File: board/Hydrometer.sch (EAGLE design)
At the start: 13 parts, among them IC2 REG1117

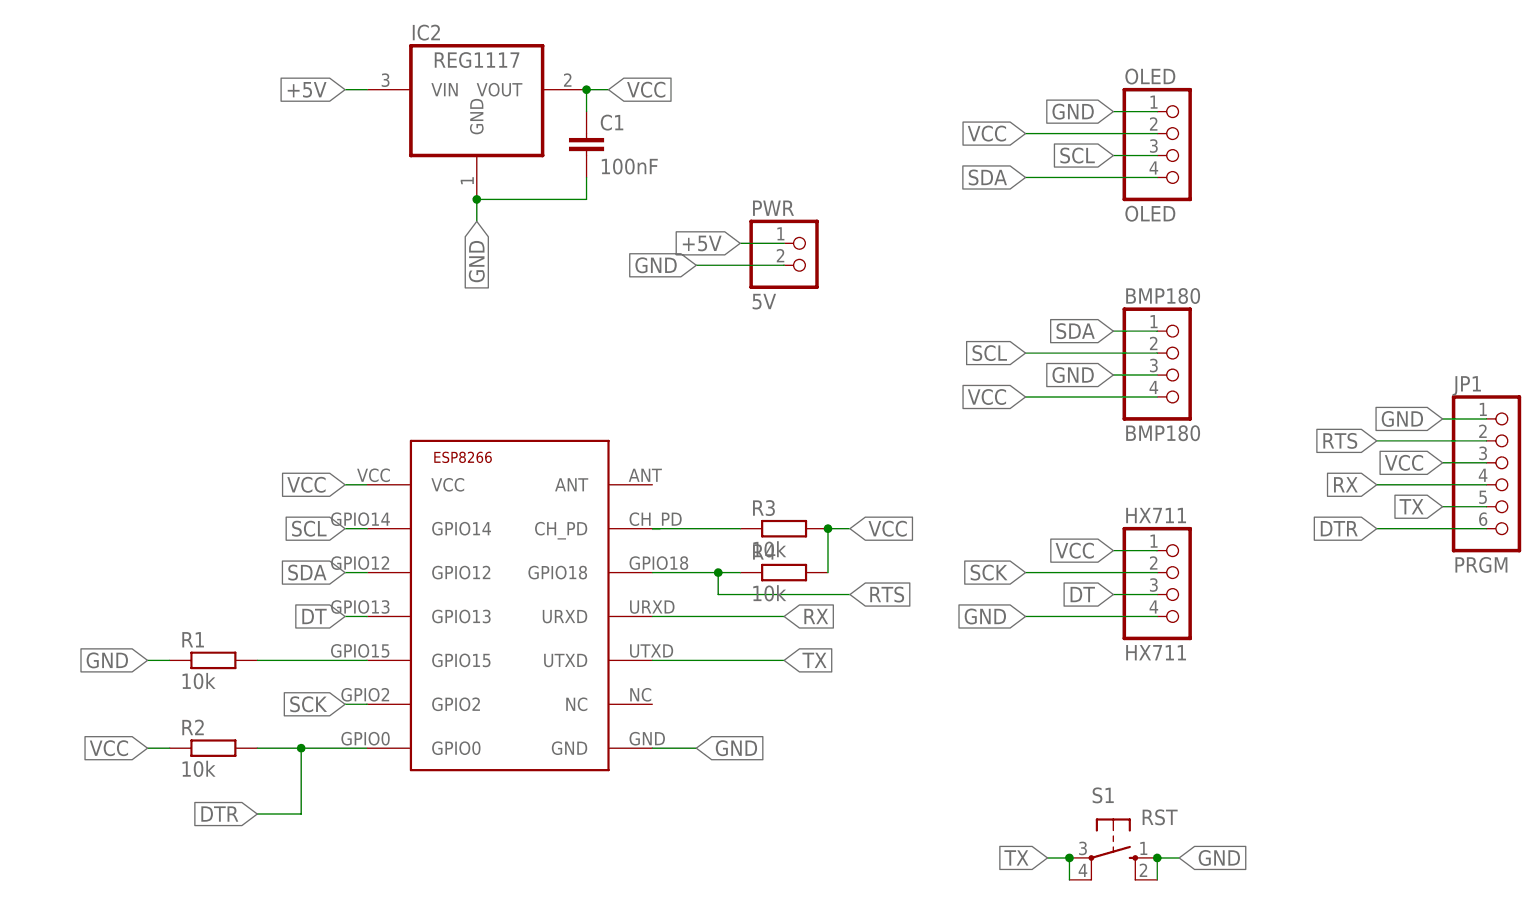
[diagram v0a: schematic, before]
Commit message: Update board layout to a (mostly) single sided PCB
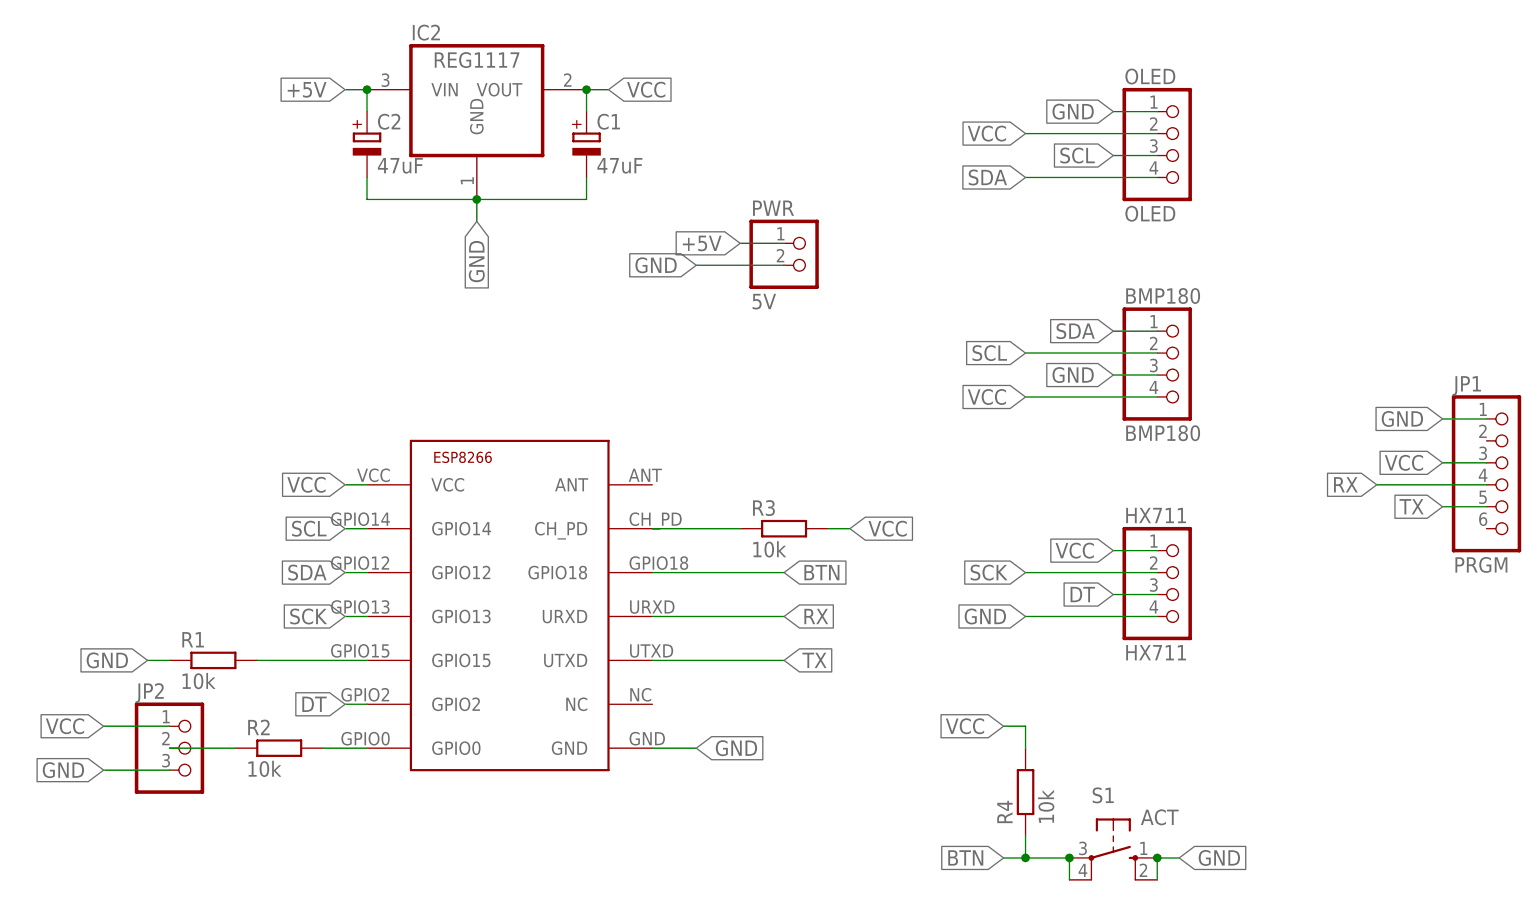
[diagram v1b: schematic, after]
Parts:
- added C2: 47uF, resistor:CPOL-EUE2.5-5
- added JP2: (no value), pinhead:PINHD-1X3
- C1: value 100nF -> 47uF; device resistor:C-EUC1206 -> resistor:CPOL-EUE2-5
- R1, R2, R3, R4: device resistor:R-EU_M1206 -> resistor:R-EU_R1206
- S1: value RST -> ACT
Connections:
- removed net RTS: JP1.2, R4.1, U$1.GPIO18
- new net BTN: R4.1, S1.P, S1.P1, U$1.GPIO18
- new net N$2: JP2.2, R2.1
- net +5V: now also C2.+
- net DT: now also U$1.GPIO2; no longer U$1.GPIO13
- net DTR: no longer JP1.6
- net GND: now also C1.-, C2.-, JP2.3; no longer C1.2
- net SCK: now also U$1.GPIO13; no longer U$1.GPIO2
- net TX: no longer S1.P, S1.P1
- net VCC: now also C1.+, JP2.1; no longer C1.1, R2.1
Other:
- moved on the sheet: R2, R4

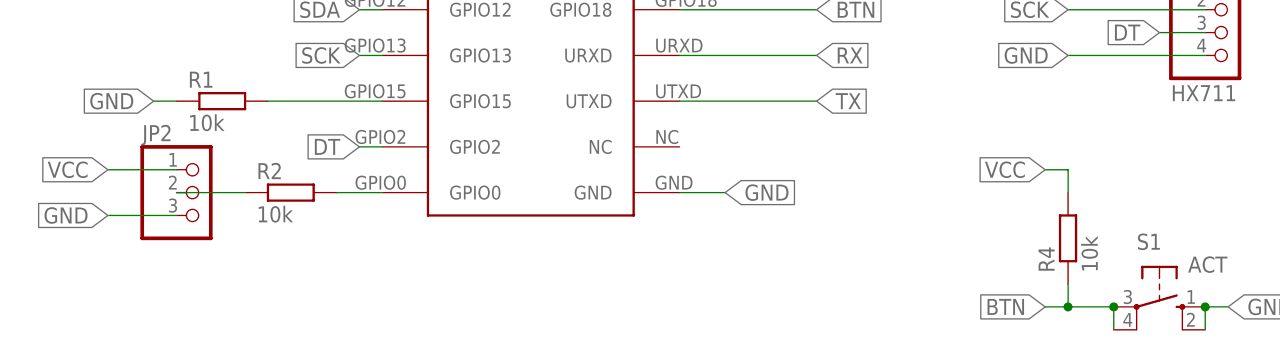
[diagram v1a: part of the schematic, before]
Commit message: Add fill planes to board
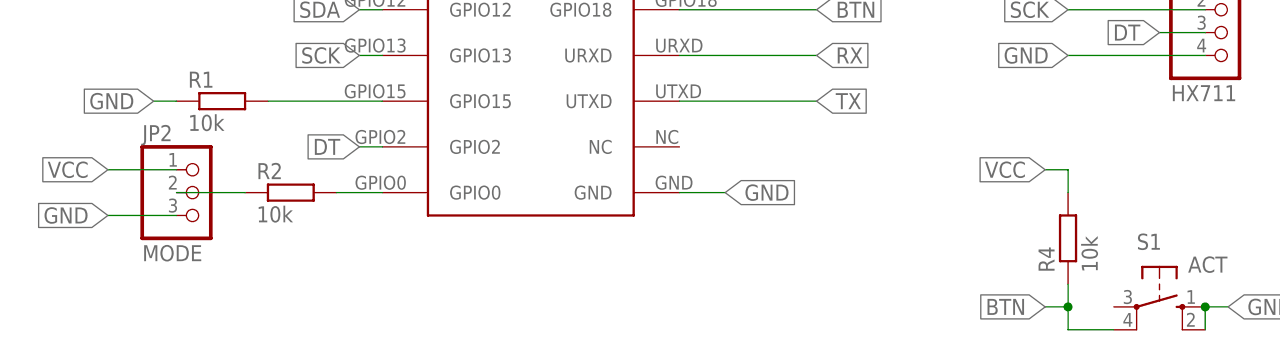
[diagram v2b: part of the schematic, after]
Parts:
- JP2: value (none) -> MODE
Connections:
- net BTN: no longer S1.P
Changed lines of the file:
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@@
 <grid distance="0.1" unitdist="inch" unit="inch" style="lines" multiple="1" display="no" altdistance="0.01" altunitdist="inch" altunit="inch"/>
 <layers>
-<layer number="1" name="Top" color="4" fill="1" visible="yes" active="no"/>
-<layer number="16" name="Bottom" color="1" fill="1" visible="yes" active="no"/>
-<layer number="17" name="Pads" color="2" fill="1" visible="yes" active="no"/>
-<layer number="18" name="Vias" color="2" fill="1" visible="yes" active="no"/>
-<layer number="19" name="Unrouted" color="6" fill="1" visible="yes" active="no"/>
-<layer number="20" name="Dimension" color="15" fill="1" visible="yes" active="no"/>
-<layer number="21" name="tPlace" color="7" fill="1" visible="yes" active="no"/>
-<layer number="22" name="bPlace" color="7" fill="1" visible="yes" active="no"/>
-<layer number="23" name="tOrigins" color="15" fill="1" visible="yes" active="no"/>
-<layer number="24" name="bOrigins" color="15" fill="1" visible="yes" active="no"/>
-<layer number="25" name="tNames" color="7" fill="1" visible="yes" active="no"/>
-<layer number="26" name="bNames" color="7" fill="1" visible="yes" active="no"/>
-<layer number="27" name="tValues" color="7" fill="1" visible="yes" active="no"/>
-<layer number="28" name="bValues" color="7" fill="1" visible="yes" active="no"/>
+<layer number="1" name="Top" color="4" fill="1" visible="no" active="no"/>
+<layer number="16" name="Bottom" color="1" fill="1" visible="no" active="no"/>
+<layer number="17" name="Pads" color="2" fill="1" visible="no" active="no"/>
+<layer number="18" name="Vias" color="2" fill="1" visible="no" active="no"/>
+<layer number="19" name="Unrouted" color="6" fill="1" visible="no" active="no"/>
+<layer number="20" name="Dimension" color="15" fill="1" visible="no" active="no"/>
+<layer number="21" name="tPlace" color="7" fill="1" visible="no" active="no"/>
+<layer number="22" name="bPlace" color="7" fill="1" visible="no" active="no"/>
+<layer number="23" name="tOrigins" color="15" fill="1" visible="no" active="no"/>
+<layer number="24" name="bOrigins" color="15" fill="1" visible="no" active="no"/>
+<layer number="25" name="tNames" color="7" fill="1" visible="no" active="no"/>
+<layer number="26" name="bNames" color="7" fill="1" visible="no" active="no"/>
+<layer number="27" name="tValues" color="7" fill="1" visible="no" active="no"/>
+<layer number="28" name="bValues" color="7" fill="1" visible="no" active="no"/>
 <layer number="29" name="tStop" color="7" fill="3" visible="no" active="no"/>
 <layer number="30" name="bStop" color="7" fill="6" visible="no" active="no"/>
@@
 <layer number="35" name="tGlue" color="7" fill="4" visible="no" active="no"/>
 <layer number="36" name="bGlue" color="7" fill="5" visible="no" active="no"/>
-<layer number="37" name="tTest" color="7" fill="1" visible="yes" active="no"/>
-<layer number="38" name="bTest" color="7" fill="1" visible="yes" active="no"/>
+<layer number="37" name="tTest" color="7" fill="1" visible="no" active="no"/>
+<layer number="38" name="bTest" color="7" fill="1" visible="no" active="no"/>
 <layer number="39" name="tKeepout" color="4" fill="11" visible="no" active="no"/>
 <layer number="40" name="bKeepout" color="1" fill="11" visible="no" active="no"/>
@@
 <layer number="44" name="Drills" color="7" fill="1" visible="no" active="no"/>
 <layer number="45" name="Holes" color="7" fill="1" visible="no" active="no"/>
-<layer number="46" name="Milling" color="3" fill="1" visible="yes" active="no"/>
-<layer number="47" name="Measures" color="7" fill="1" visible="yes" active="no"/>
-<layer number="48" name="Document" color="7" fill="1" visible="yes" active="no"/>
-<layer number="49" name="Reference" color="7" fill="1" visible="yes" active="no"/>
-<layer number="51" name="tDocu" color="7" fill="1" visible="yes" active="no"/>
-<layer number="52" name="bDocu" color="7" fill="1" visible="yes" active="no"/>
+<layer number="46" name="Milling" color="3" fill="1" visible="no" active="no"/>
+<layer number="47" name="Measures" color="7" fill="1" visible="no" active="no"/>
+<layer number="48" name="Document" color="7" fill="1" visible="no" active="no"/>
+<layer number="49" name="Reference" color="7" fill="1" visible="no" active="no"/>
+<layer number="51" name="tDocu" color="7" fill="1" visible="no" active="no"/>
+<layer number="52" name="bDocu" color="7" fill="1" visible="no" active="no"/>
 <layer number="90" name="Modules" color="5" fill="1" visible="yes" active="yes"/>
 <layer number="91" name="Nets" color="2" fill="1" visible="yes" active="yes"/>
@@
 <part name="C2" library="resistor" deviceset="CPOL-EU" device="E2.5-5" value="47uF"/>
 <part name="R4" library="resistor" deviceset="R-EU_" device="R1206" value="10k"/>
-<part name="JP2" library="pinhead" deviceset="PINHD-1X3" device=""/>
+<part name="JP2" library="pinhead" deviceset="PINHD-1X3" device="" value="MODE"/>
 </parts>
 <sheets>
@@
 <net name="BTN" class="0">
 <segment>
-<pinref part="S1" gate="1" pin="P1"/>
-<pinref part="S1" gate="1" pin="P"/>
-<wire x1="43.18" y1="27.94" x2="43.18" y2="30.48" width="0.1524" layer="91"/>
-<wire x1="43.18" y1="30.48" x2="38.1" y2="30.48" width="0.1524" layer="91"/>
-<junction x="43.18" y="30.48"/>
 <label x="35.56" y="30.48" size="1.778" layer="95" rot="MR0" xref="yes"/>
 <pinref part="R4" gate="G$1" pin="1"/>
 <wire x1="38.1" y1="30.48" x2="35.56" y2="30.48" width="0.1524" layer="91"/>
 <wire x1="38.1" y1="33.02" x2="38.1" y2="30.48" width="0.1524" layer="91"/>
+<wire x1="38.1" y1="30.48" x2="38.1" y2="27.94" width="0.1524" layer="91"/>
+<pinref part="S1" gate="1" pin="P1"/>
+<wire x1="38.1" y1="27.94" x2="43.18" y2="27.94" width="0.1524" layer="91"/>
 <junction x="38.1" y="30.48"/>
 </segment>
